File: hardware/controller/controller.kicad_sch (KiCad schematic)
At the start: 18 parts, among them U1 ESP32-S3-DEVKITC-1-N8R8

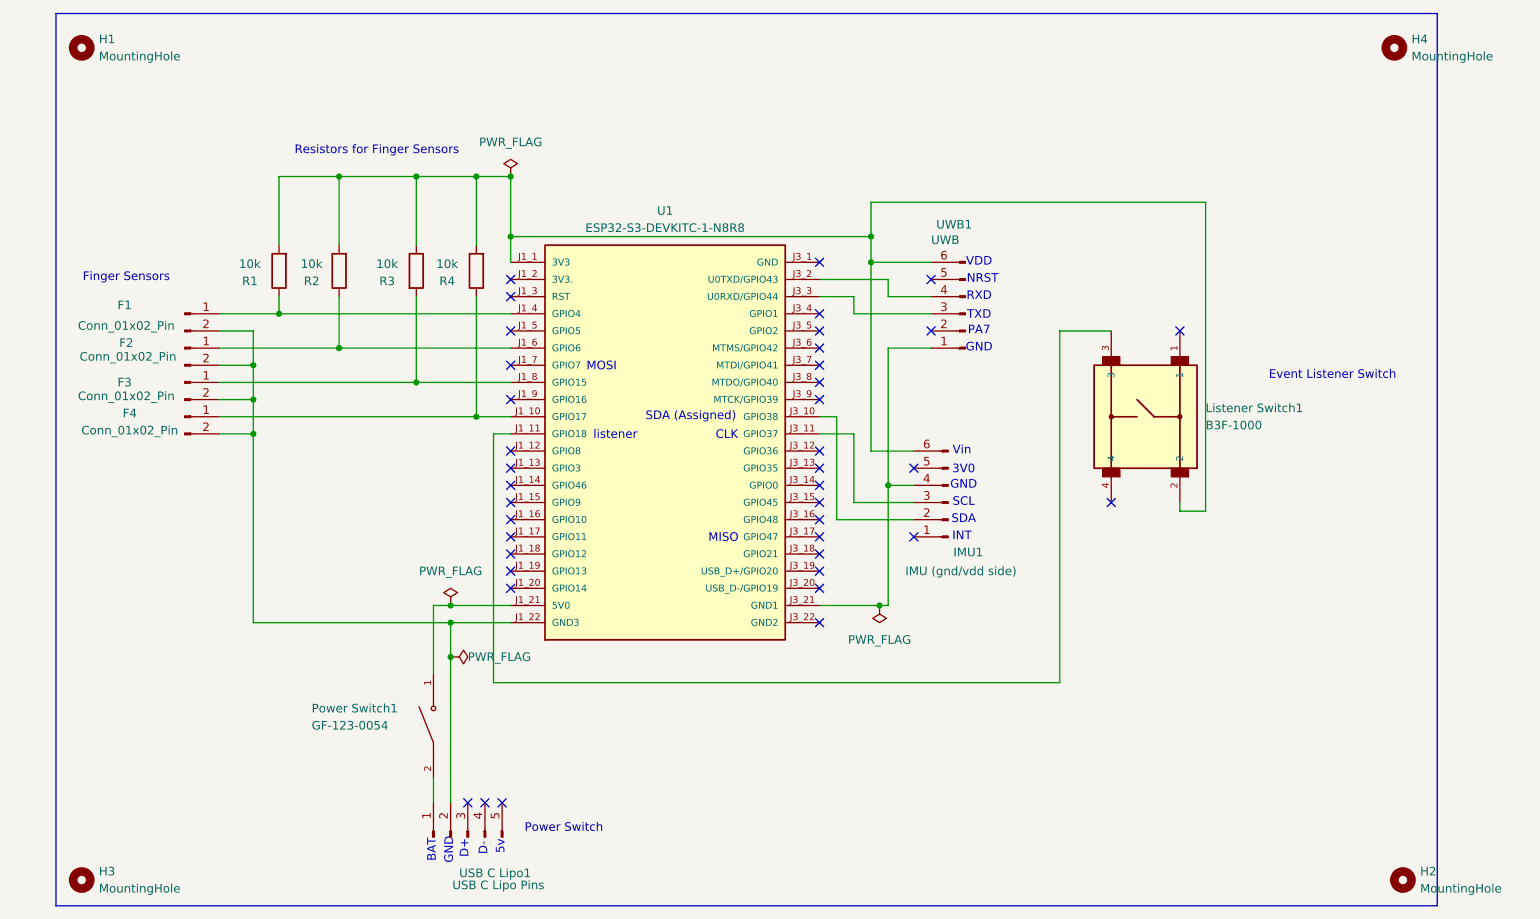
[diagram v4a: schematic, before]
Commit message: kinda a shitshow, need to reroute after adding terminal blocks
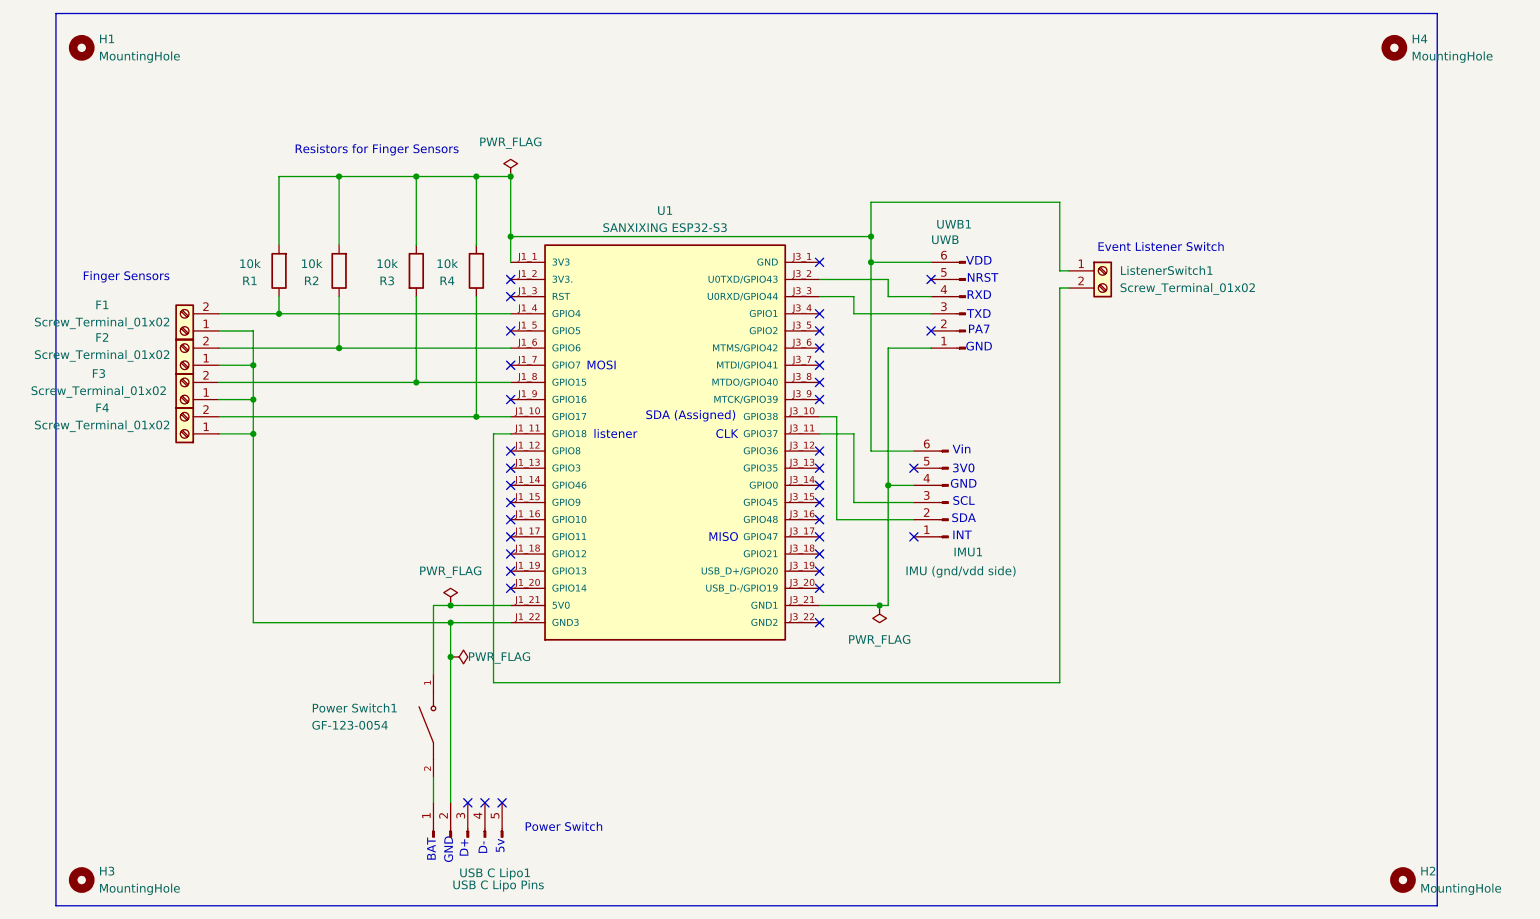
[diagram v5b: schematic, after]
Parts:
- removed F1, F2, F3, F4: Conn_01x02_Pin, Connector_PinSocket_2.54mm:PinSocket_1x02_P2.54mm_Vertical, symbol Connector:Conn_01x02_Pin
- removed Listener Switch1: B3F-1000, Omron Tactile Button Small B3f-1000:SW_B3F-1000, symbol Omron Tactile Button Small:B3F-1000
- added F1, F2, F3, F4, ListenerSwitch1: Screw_Terminal_01x02, TerminalBlock:TerminalBlock_MaiXu_MX126-5.0-02P_1x02_P5.00mm, symbol Connector:Screw_Terminal_01x02
- U1: value ESP32-S3-DEVKITC-1-N8R8 -> SANXIXING ESP32-S3; footprint SANXIXING ESP32-S3:ESP32-S3-DEVKITC-1-N8R8 -> SANXIXING ESP32-S3:SANXIXING-ESP32-S3
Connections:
- net at R3.2, U1.J1_8 (GPIO15): now also F3.2 (Pin_2)
- net at U1.J1_22 (GND3), USB C Lipo1.2 (Pin_2): now also F1.1 (Pin_1), F2.1 (Pin_1), F3.1 (Pin_1), F4.1 (Pin_1)
- net at IMU1.6 (Pin_6), R1.2, R2.2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: now also ListenerSwitch1.1 (Pin_1)
- net at U1.J1_11 (GPIO18): now also ListenerSwitch1.2 (Pin_2)
- net at R1.1, U1.J1_4 (GPIO4): now also F1.2 (Pin_2)
- net at R2.1, U1.J1_6 (GPIO6): now also F2.2 (Pin_2)
- net at R4.1, U1.J1_10 (GPIO17): now also F4.2 (Pin_2)
- no-connect marks 40 -> 38

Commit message: Changing power pins for battery
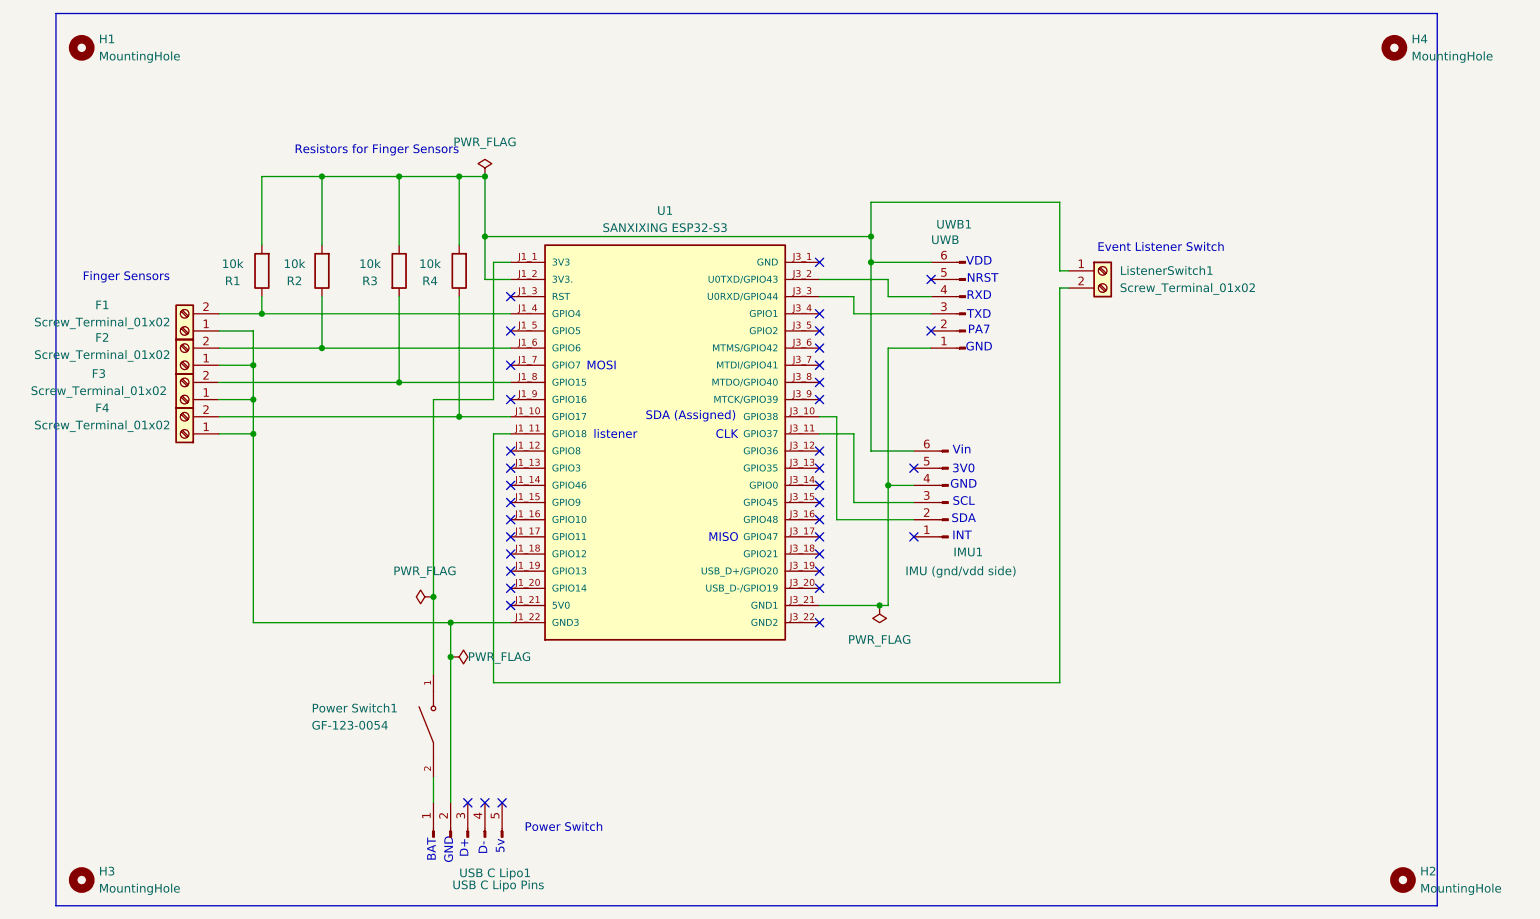
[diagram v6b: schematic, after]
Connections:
- net at IMU1.6 (Pin_6), ListenerSwitch1.1 (Pin_1), R1.2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: now also U1.J1_2 (3V3.); no longer U1.J1_1 (3V3)
- net at Power Switch1.1: now also U1.J1_1 (3V3); no longer U1.J1_21 (5V0)
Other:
- moved on the sheet: R1, R2, R3, R4

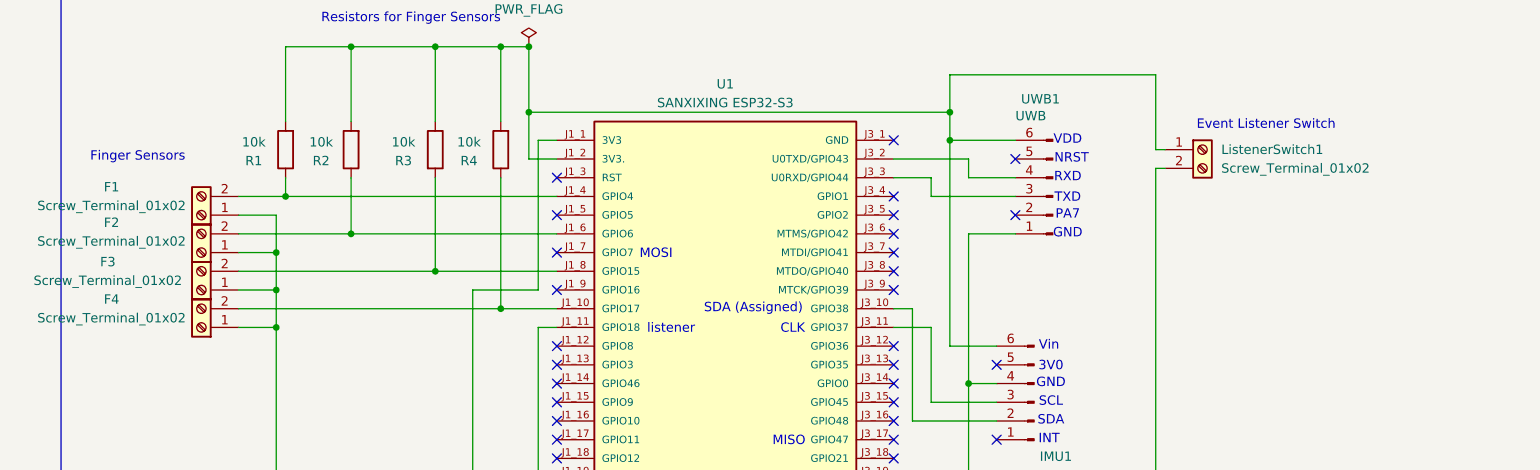
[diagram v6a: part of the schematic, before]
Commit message: routing and placing checkpoint, should be ready for fab
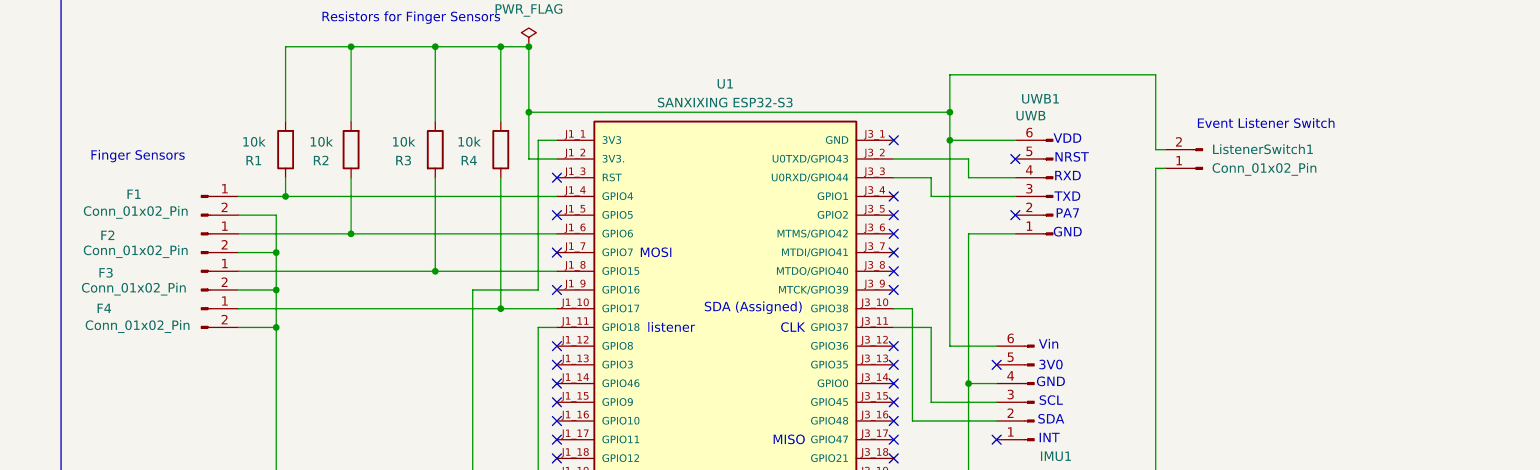
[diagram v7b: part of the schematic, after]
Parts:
- removed F1, F2, F3, F4, ListenerSwitch1: Screw_Terminal_01x02, TerminalBlock:TerminalBlock_MaiXu_MX126-5.0-02P_1x02_P5.00mm, symbol Connector:Screw_Terminal_01x02
- added F1, F2, F3, F4, ListenerSwitch1: Conn_01x02_Pin, Connector_PinSocket_2.54mm:PinSocket_1x02_P2.54mm_Vertical, symbol Connector:Conn_01x02_Pin
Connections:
- net at R4.1, U1.J1_10 (GPIO17): now also F4.1 (Pin_1)
- net at U1.J1_11 (GPIO18): now also ListenerSwitch1.1 (Pin_1)
- net at IMU1.6 (Pin_6), R1.2, R2.2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: now also ListenerSwitch1.2 (Pin_2)
- net at U1.J1_22 (GND3), USB C Lipo1.2 (Pin_2): now also F1.2 (Pin_2), F2.2 (Pin_2), F3.2 (Pin_2), F4.2 (Pin_2)
- net at R1.1, U1.J1_4 (GPIO4): now also F1.1 (Pin_1)
- net at R2.1, U1.J1_6 (GPIO6): now also F2.1 (Pin_1)
- net at R3.2, U1.J1_8 (GPIO15): now also F3.1 (Pin_1)
